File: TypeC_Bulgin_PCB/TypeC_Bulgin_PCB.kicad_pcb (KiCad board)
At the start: 2 copper layers, 16.1 x 16.1 mm, 4 parts, among them J1 Conn_01x01_Female, J3 Conn_01x13, J4 Conn_01x13, J6 USB_C_Receptacle

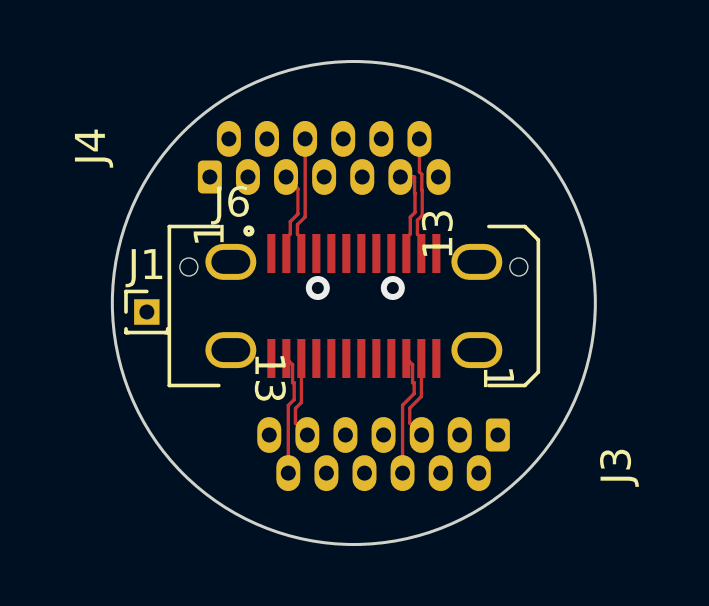
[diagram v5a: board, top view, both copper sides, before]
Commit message: v0.93 differential pairs were routed and equalised, polydons were placed
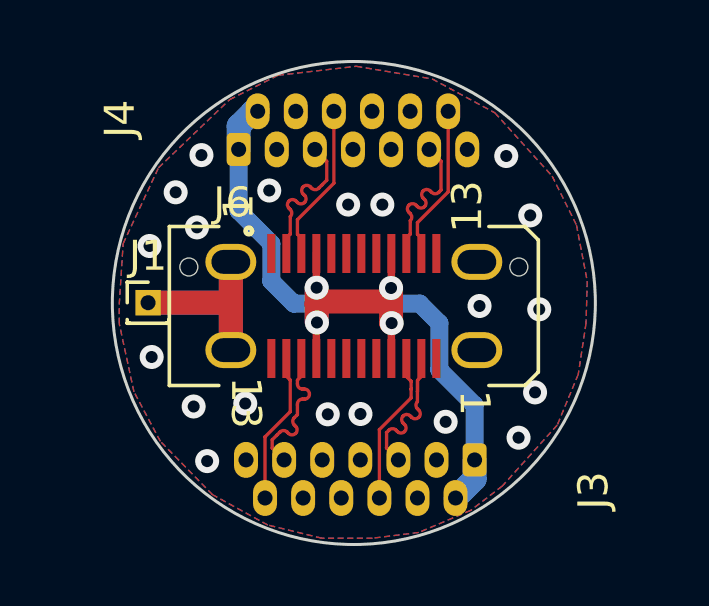
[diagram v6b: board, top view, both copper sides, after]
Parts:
- moved J4 1.33 mm to (147.4, 82.3)
- moved J3 1.14 mm to (155.2, 92.6)
- moved J1 0.31 mm to (144.3, 87.4)
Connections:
- J1 pad 1: unconnected-(J1-Pad1) -> Net-(J1-Pad1)
- J6 pad S1: unconnected-(J6-PadS1) -> Net-(J1-Pad1)
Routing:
- net VBUS: track 0.00 -> 30.5 mm, vias 0 -> 4
- net Net-(J1-Pad1): track 0.00 -> 11.5 mm
- net TX2+: track 2.87 -> 5.16 mm
- net TX1+: track 2.87 -> 4.99 mm
- net RX1-: track 2.80 -> 4.92 mm
- net RX2-: track 3.15 -> 5.08 mm
- net TX2-: track 3.98 -> 5.30 mm
- net RX2+: track 3.98 -> 5.22 mm
- net TX1-: track 4.12 -> 5.16 mm
- net RX1+: track 4.04 -> 5.05 mm
- net GND: vias 0 -> 20
- net (no net): vias 2 -> 0
- added copper zone on B.Cu, net GND
- added copper zone on F.Cu, net GND
